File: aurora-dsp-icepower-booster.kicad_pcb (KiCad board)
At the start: 2 copper layers, 200 x 200 mm, 243 parts, among them J1 XLR_IN_1, J10 XLR3_OUT, J11 XLR3_OUT, J12 XLR3_OUT, J13 24V DC, J14 REMOTE 3.5mm, J2 XLR_IN_2, J3 XLR_IN_3, J4 XLR_IN_4, J5 XLR_IN_5, J6 XLR_IN_6, J7 XLR3_OUT, J8 XLR3_OUT, J9 XLR3_OUT, SW1 Gain CH1, SW2 Gain CH2, SW3 Gain CH3, SW4 Gain CH4, SW5 Gain CH5, SW6 Gain CH6, SW7 ALWAYS/REMOTE, U1 LM4562, U10 LM4562, U11 LM4562, U12 LM4562, U13 TEL5-2422, U14 ADP7118ARDZ-11, U15 ADP7182AUJZ-11, U2 LM4562, U3 LM4562, U4 LM4562, U5 LM4562, U6 LM4562, U7 LM4562, U8 LM4562, U9 LM4562

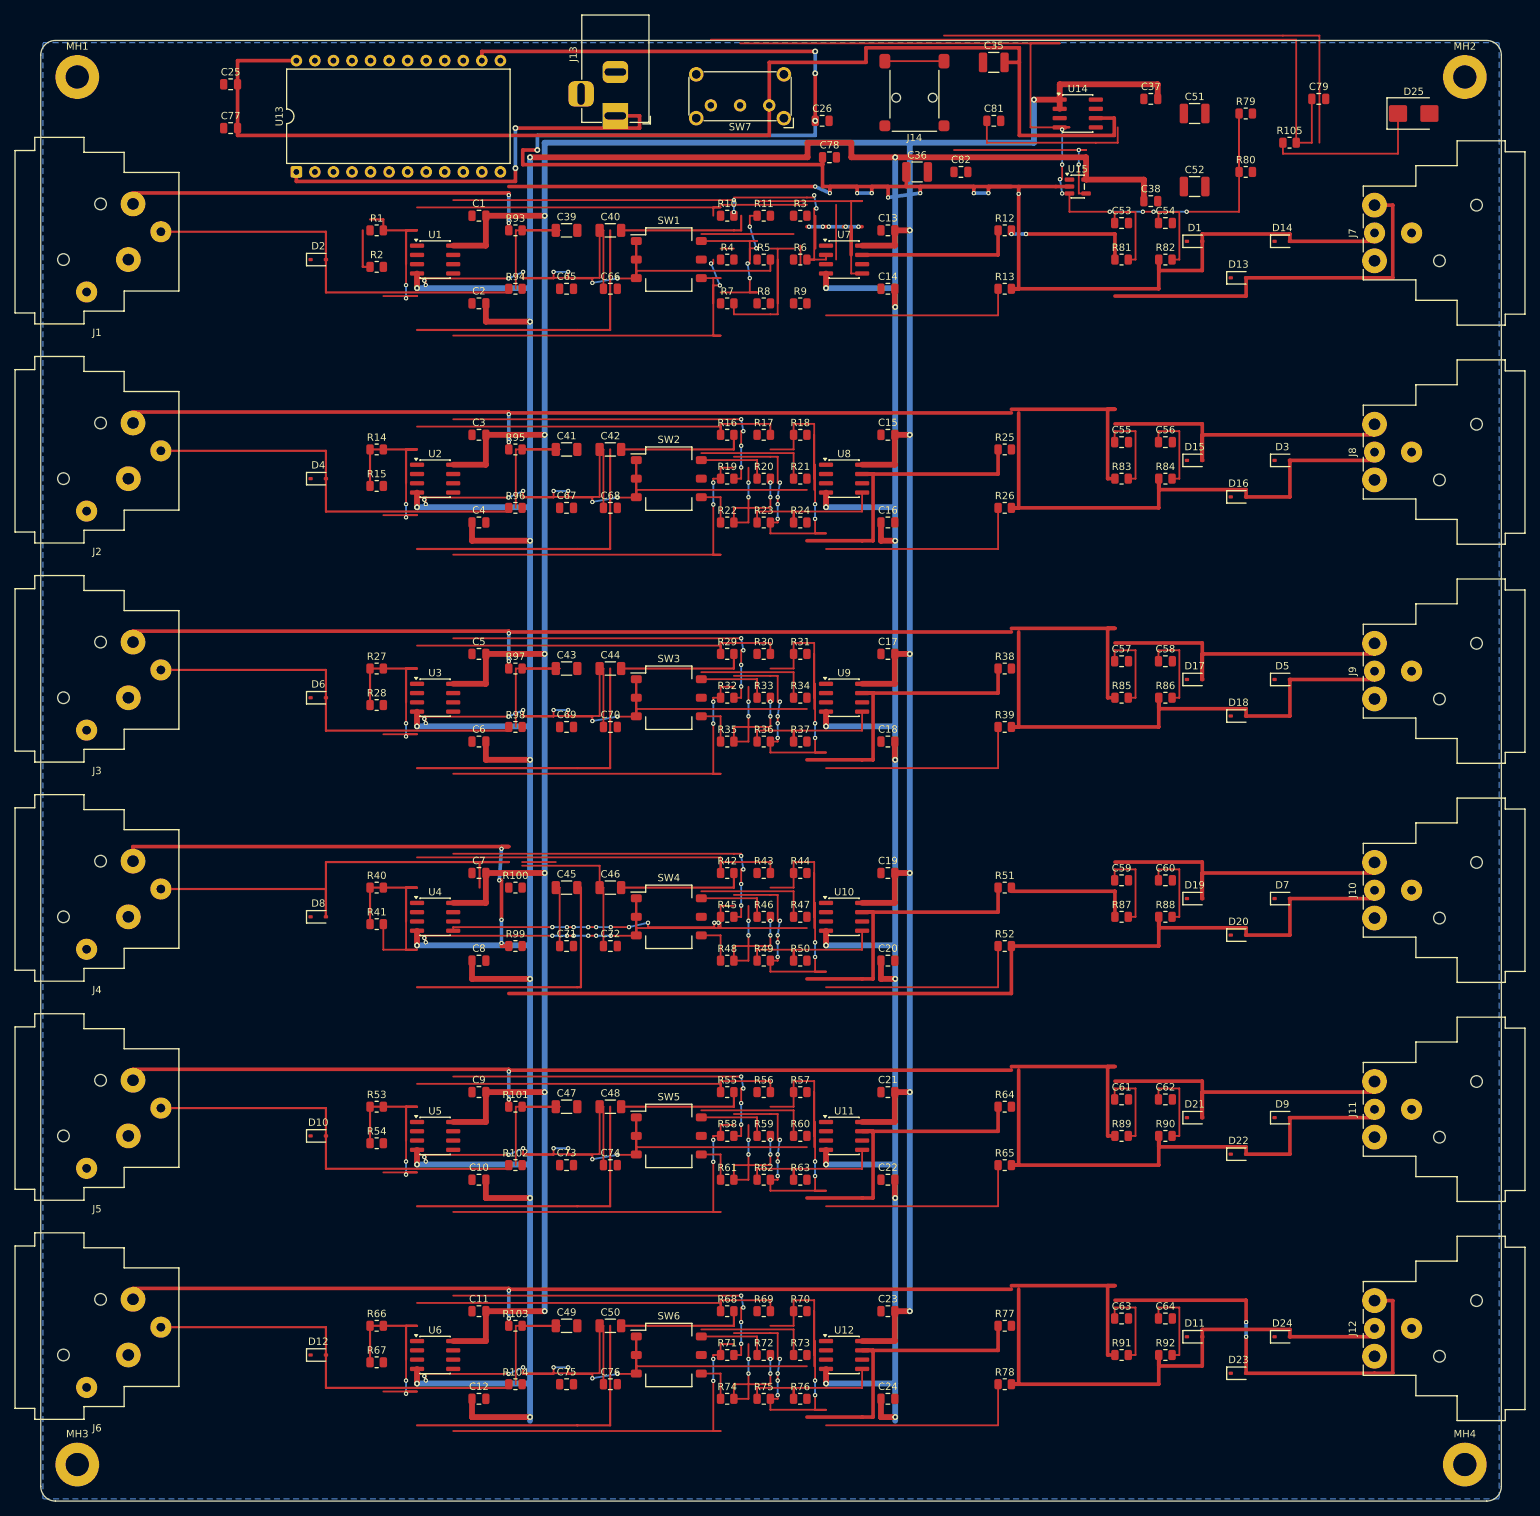
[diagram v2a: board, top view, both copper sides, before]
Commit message: Phase 2: 0 shorts, 0 crossings (54 tracks + 13 vias entfernt)
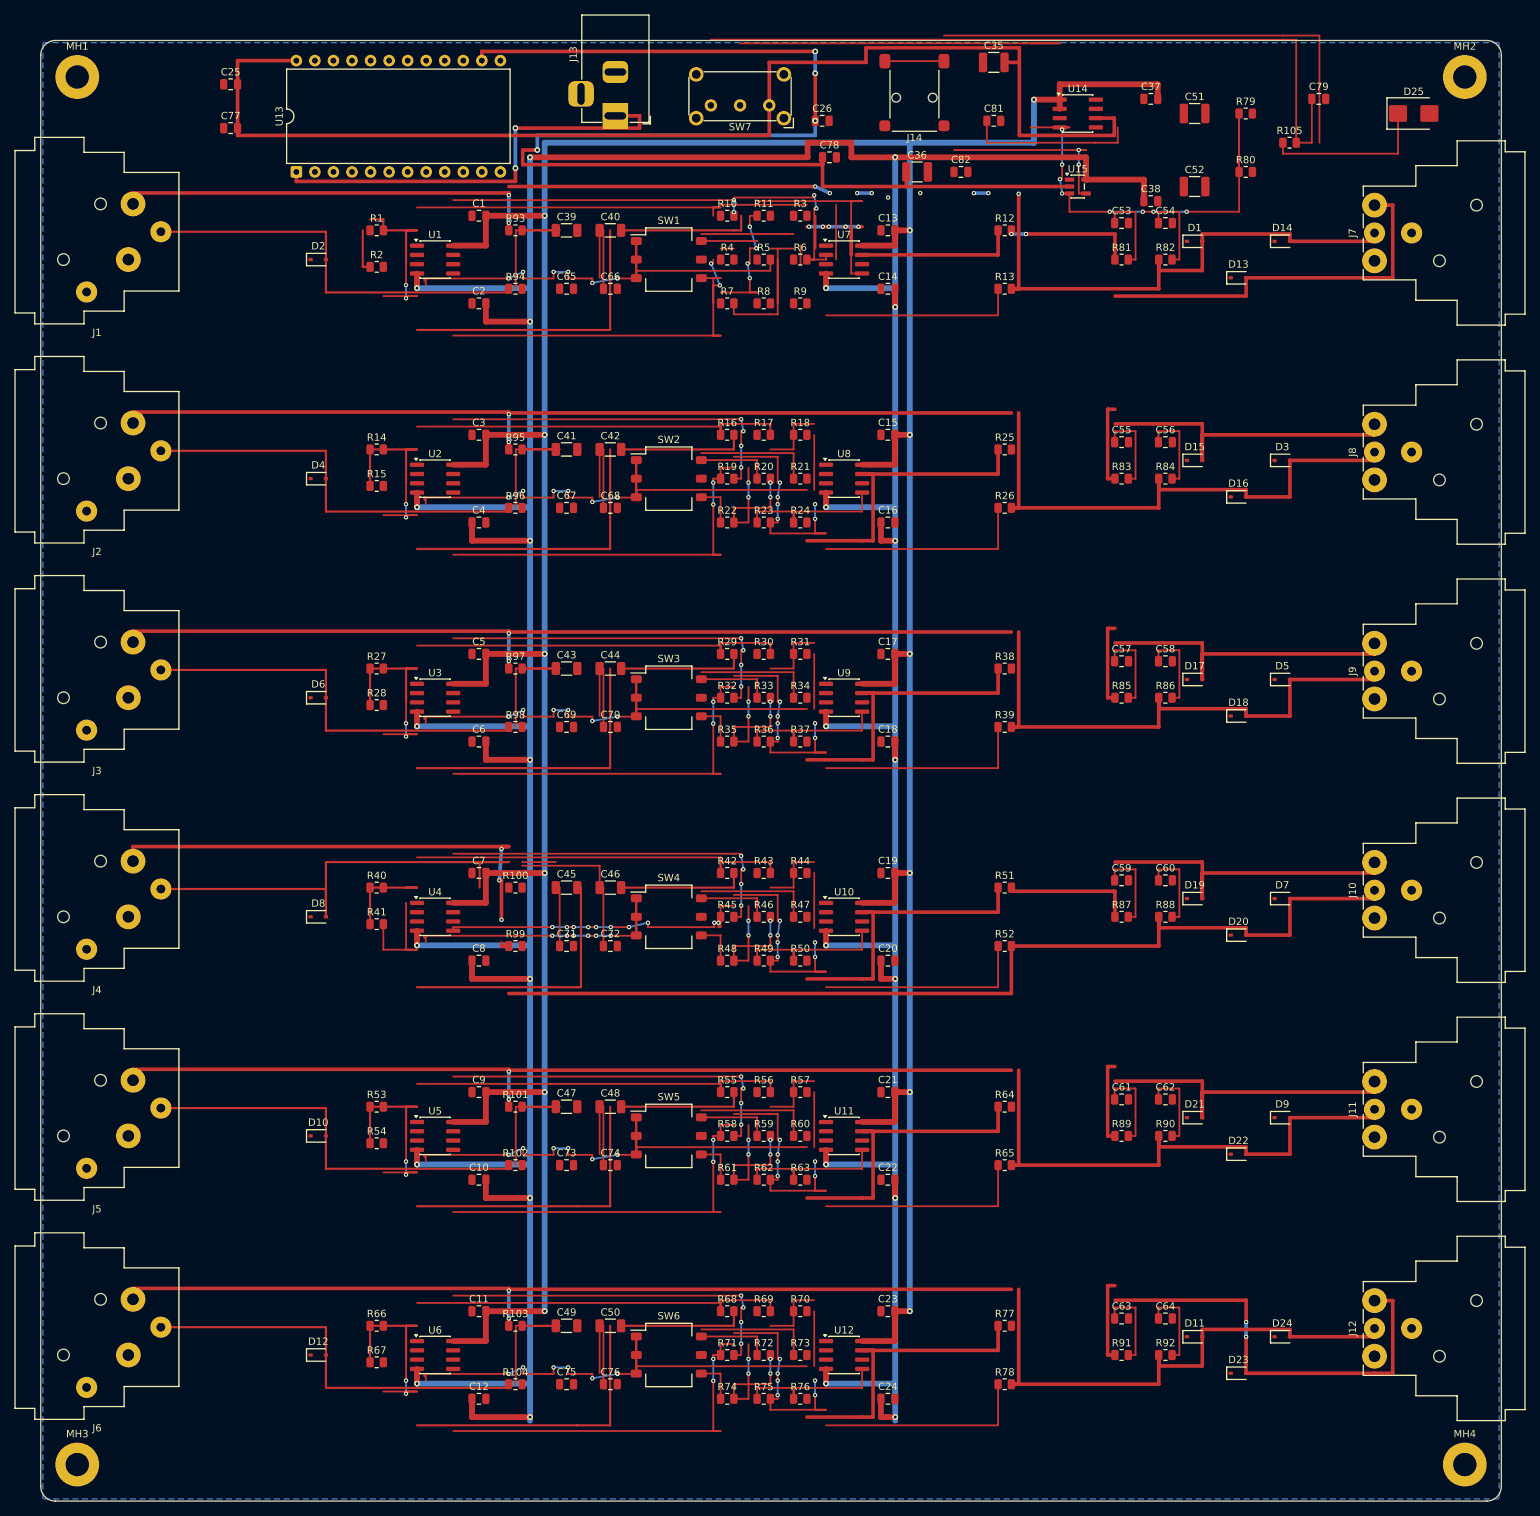
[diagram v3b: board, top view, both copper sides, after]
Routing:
- net /CH1_OUT_COLD: track 211.4 -> 182.7 mm
- net /CH4_RX_OUT: track 90.2 -> 65.0 mm, vias 8 -> 6
- net /CH6_OUT_HOT: track 86.2 -> 72.0 mm
- net /CH5_OUT_HOT: track 71.2 -> 57.0 mm
- net /CH3_OUT_HOT: track 71.2 -> 57.0 mm
- net /CH2_OUT_HOT: track 71.2 -> 57.0 mm
- net /EN_CTRL: track 123.2 -> 111.7 mm
- net /CH6_EMI_COLD: track 25.6 -> 15.0 mm
- net /CH5_EMI_COLD: track 25.6 -> 15.0 mm
- net /CH3_EMI_COLD: track 25.6 -> 15.0 mm
- net /CH2_EMI_COLD: track 25.6 -> 15.0 mm
- net /CH1_EMI_COLD: track 25.6 -> 15.0 mm
- net /CH3_SUMNODE: track 89.8 -> 82.3 mm
- net /CH6_SUMNODE: track 89.8 -> 82.3 mm
- net /CH5_SUMNODE: track 89.8 -> 82.3 mm
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
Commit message: Phase 3: 0 errors - clearance/edge frei (19 tracks entfernt)
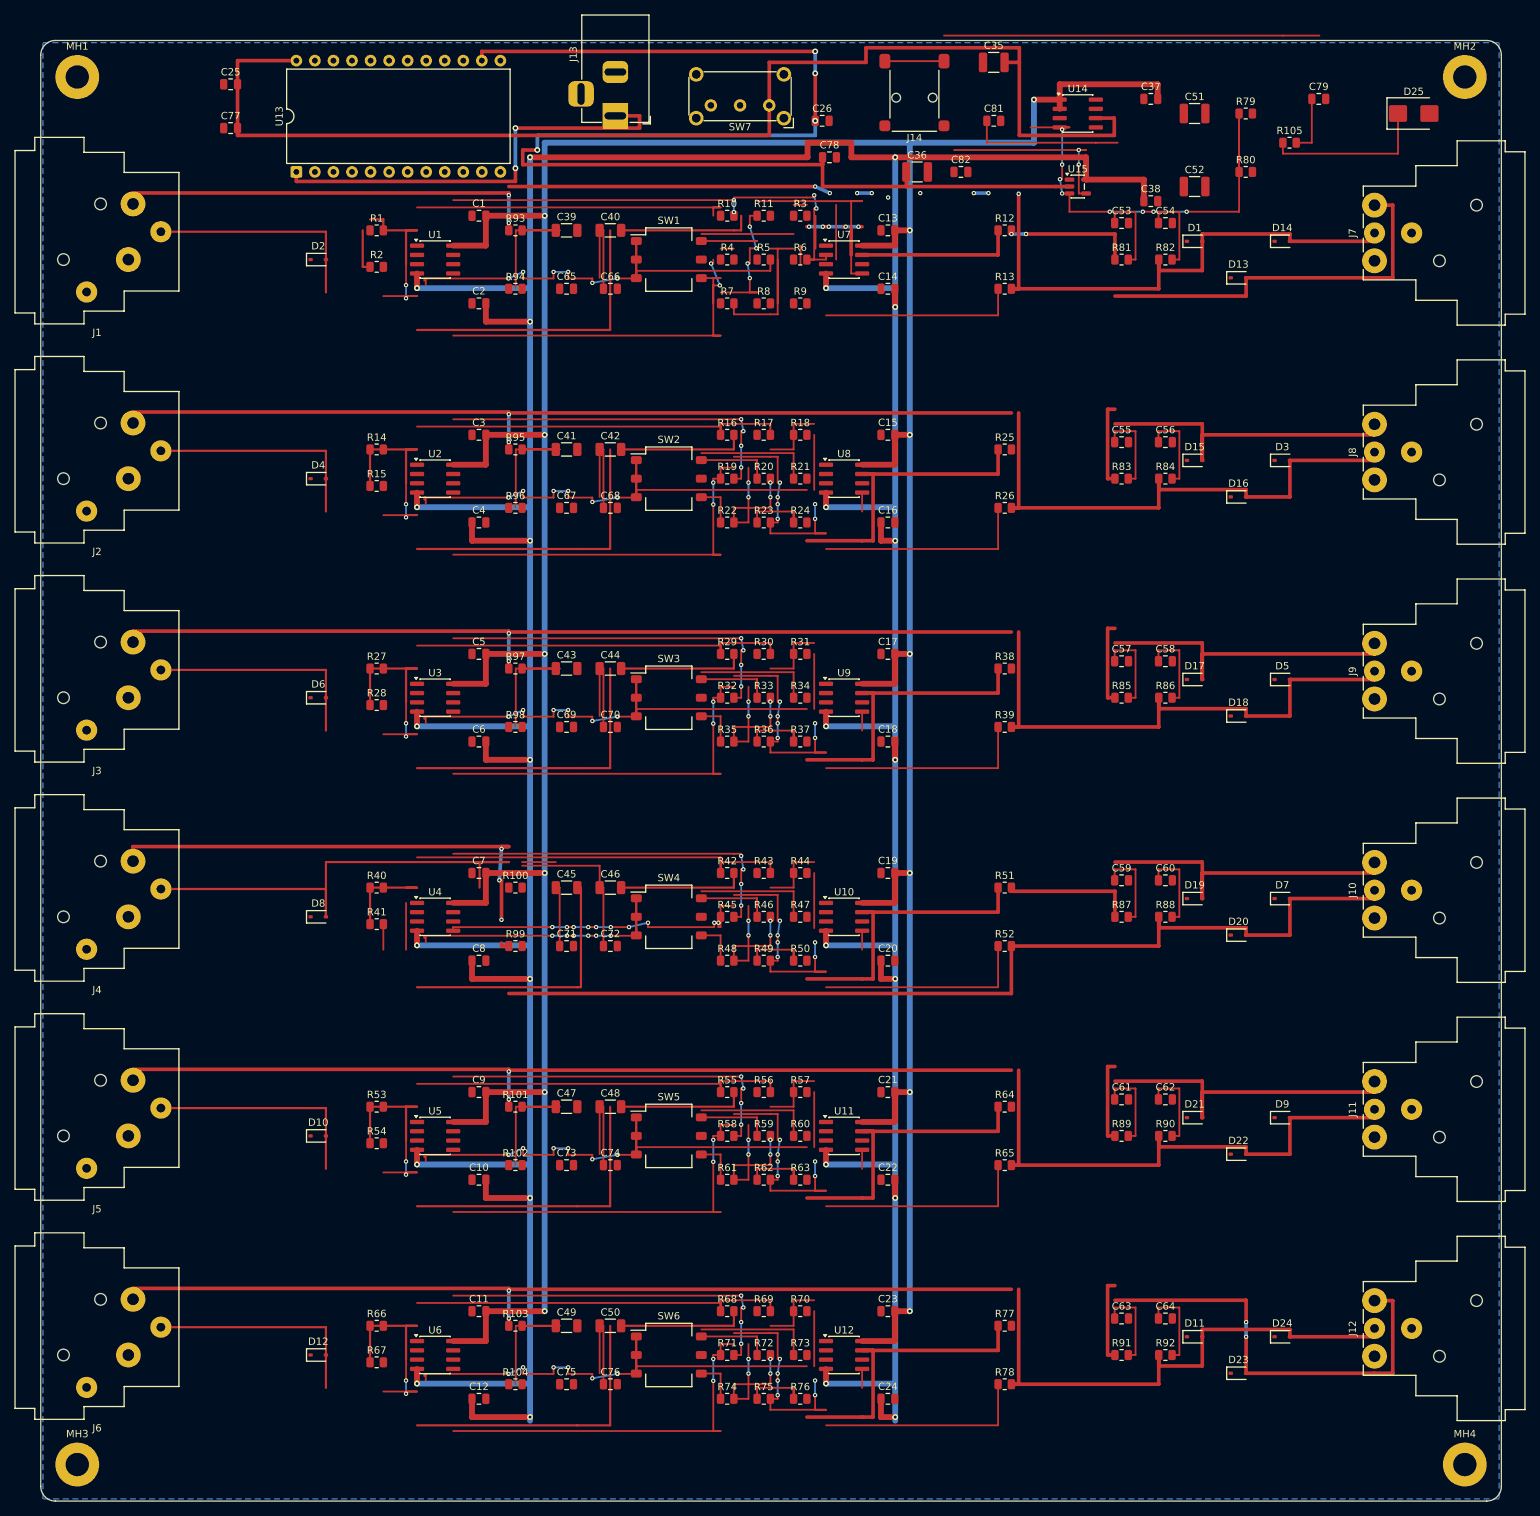
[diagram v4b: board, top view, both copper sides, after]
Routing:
- net /REMOTE_FILT: track 102.4 -> 8.14 mm
- net /EN_CTRL: track 111.7 -> 63.9 mm
- net /CH1_COLD_RAW: track 56.5 -> 31.4 mm
- net /CH6_COLD_RAW: track 56.5 -> 31.4 mm
- net /CH5_COLD_RAW: track 56.5 -> 31.4 mm
- net /CH3_COLD_RAW: track 56.5 -> 31.4 mm
- net /CH2_COLD_RAW: track 56.5 -> 31.4 mm
- net /REMOTE_IN: track 96.9 -> 82.3 mm
- net /CH1_SUMNODE: track 46.8 -> 36.8 mm
- net /CH6_GAIN_FB: track 21.5 -> 12.1 mm
- net /CH5_GAIN_FB: track 21.5 -> 12.1 mm
- net /CH4_GAIN_FB: track 21.5 -> 12.1 mm
- net /CH3_GAIN_FB: track 21.5 -> 12.1 mm
- net /CH2_GAIN_FB: track 21.5 -> 12.1 mm
- net /CH4_RX_OUT: track 65.0 -> 58.9 mm
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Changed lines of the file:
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@@
 	)
 	(segment
-		(start 39.05 34.5)
-		(end 64.09 34.5)
-		(width 0.3)
-		(layer "F.Cu")
-		(net 6)
-	)
-	(segment
 		(start 64.09 34)
 		(end 64.09 34.5)
@@
 	)
 	(segment
-		(start 93.09 22.5)
-		(end 103.09 22.5)
-		(width 0.25)
-		(layer "F.Cu")
-		(net 19)
-	)
-	(segment
 		(start 108.91 22.5)
 		(end 108.91 30)
@@
 	)
 	(segment
-		(start 39.05 64.5)
-		(end 64.09 64.5)
-		(width 0.3)
-		(layer "F.Cu")
-		(net 25)
-	)
-	(segment
 		(start 64.09 64)
 		(end 64.09 64.5)
@@
 	)
 	(segment
-		(start 103.09 64.5)
-		(end 112.47 64.5)
-		(width 0.25)
-		(layer "F.Cu")
-		(net 28)
-	)
-	(segment
 		(start 112.47 61.91)
 		(end 112.47 64.5)
@@
 	)
 	(segment
-		(start 39.05 94.5)
-		(end 64.09 94.5)
-		(width 0.3)
-		(layer "F.Cu")
-		(net 44)
-	)
-	(segment
 		(start 16.45 86.19)
 		(end 39.05 86.19)
@@
 	)
 	(segment
-		(start 103.09 94.5)
-		(end 112.47 94.5)
-		(width 0.25)
-		(layer "F.Cu")
-		(net 47)
-	)
-	(segment
 		(start 100.91 90.54)
 		(end 101.21 90.54)
@@
 	)
 	(segment
-		(start 103.09 124.5)
-		(end 112.47 124.5)
-		(width 0.25)
-		(layer "F.Cu")
-		(net 66)
-	)
-	(segment
 		(start 98.09 126)
 		(end 98.09 124.5)
@@
 	)
 	(segment
-		(start 46.91 124.5)
-		(end 51.52 124.5)
-		(width 0.25)
-		(layer "F.Cu")
-		(net 75)
-	)
-	(segment
 		(start 72.05 122.59)
 		(end 72.97 122.59)
@@
 	)
 	(segment
-		(start 51.52 124.5)
-		(end 50.02 124.5)
-		(width 0.25)
-		(layer "F.Cu")
-		(net 75)
-	)
-	(segment
 		(start 46.91 121)
 		(end 46.91 124.5)
@@
 	)
 	(segment
-		(start 39.05 154.5)
-		(end 64.09 154.5)
-		(width 0.3)
-		(layer "F.Cu")
-		(net 82)
-	)
-	(segment
 		(start 39.05 150)
 		(end 39.05 154.5)
@@
 	)
 	(segment
-		(start 103.09 154.5)
-		(end 112.47 154.5)
-		(width 0.25)
-		(layer "F.Cu")
-		(net 85)
-	)
-	(segment
 		(start 100.91 155.5)
 		(end 100.91 156)
@@
 	)
 	(segment
-		(start 39.05 184.5)
-		(end 64.09 184.5)
-		(width 0.3)
-		(layer "F.Cu")
-		(net 101)
-	)
-	(segment
 		(start 16.45 176.19)
 		(end 39.05 176.19)
@@
 	)
 	(segment
-		(start 103.09 184.5)
-		(end 112.47 184.5)
-		(width 0.25)
-		(layer "F.Cu")
-		(net 104)
-	)
-	(segment
 		(start 106.03 185.5)
 		(end 106.03 187.5)
@@
 	)
 	(segment
-		(start 139.53 0.39)
-		(end 135.53 0.39)
-		(width 0.25)
-		(layer "F.Cu")
-		(net 118)
-	)
-	(segment
 		(start 140.86 23.45)
 		(end 146.38 23.45)
@@
 	)
 	(segment
-		(start 95.76 0.39)
-		(end 139.53 0.39)
-		(width 0.25)
-		(layer "F.Cu")
-		(net 118)
-	)
-	(segment
 		(start 139.86 20.95)
 		(end 140.86 20.95)
@@
 	)
 	(segment
-		(start 91.76 -0.109999)
-		(end 171.91 -0.109999)
-		(width 0.25)
-		(layer "F.Cu")
-		(net 121)
-	)
-	(segment
 		(start 174.05 8)
 		(end 174.05 14)
@@
 	)
 	(segment
-		(start 171.91 -0.109999)
-		(end 171.91 14)
-		(width 0.25)
-		(layer "F.Cu")
-		(net 121)
-	)
-	(segment
 		(start 171.91 14)
 		(end 174.05 14)
@@
 	)
 	(segment
-		(start 175.09 -0.669999)
-		(end 175.09 14)
-		(width 0.25)
-		(layer "F.Cu")
-		(net 122)
-	)
-	(segment
 		(start 185.85 10)
 		(end 185.85 15.5)
@@
 		(width 0.25)
 		(layer "F.Cu")
-		(net 123)
-	)
-	(segment
-		(start 147.47 11.9)
-		(end 147.47 14)
-		(width 0.25)
-		(layer "F.Cu")
